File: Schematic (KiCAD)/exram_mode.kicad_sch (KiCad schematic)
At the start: 77 parts

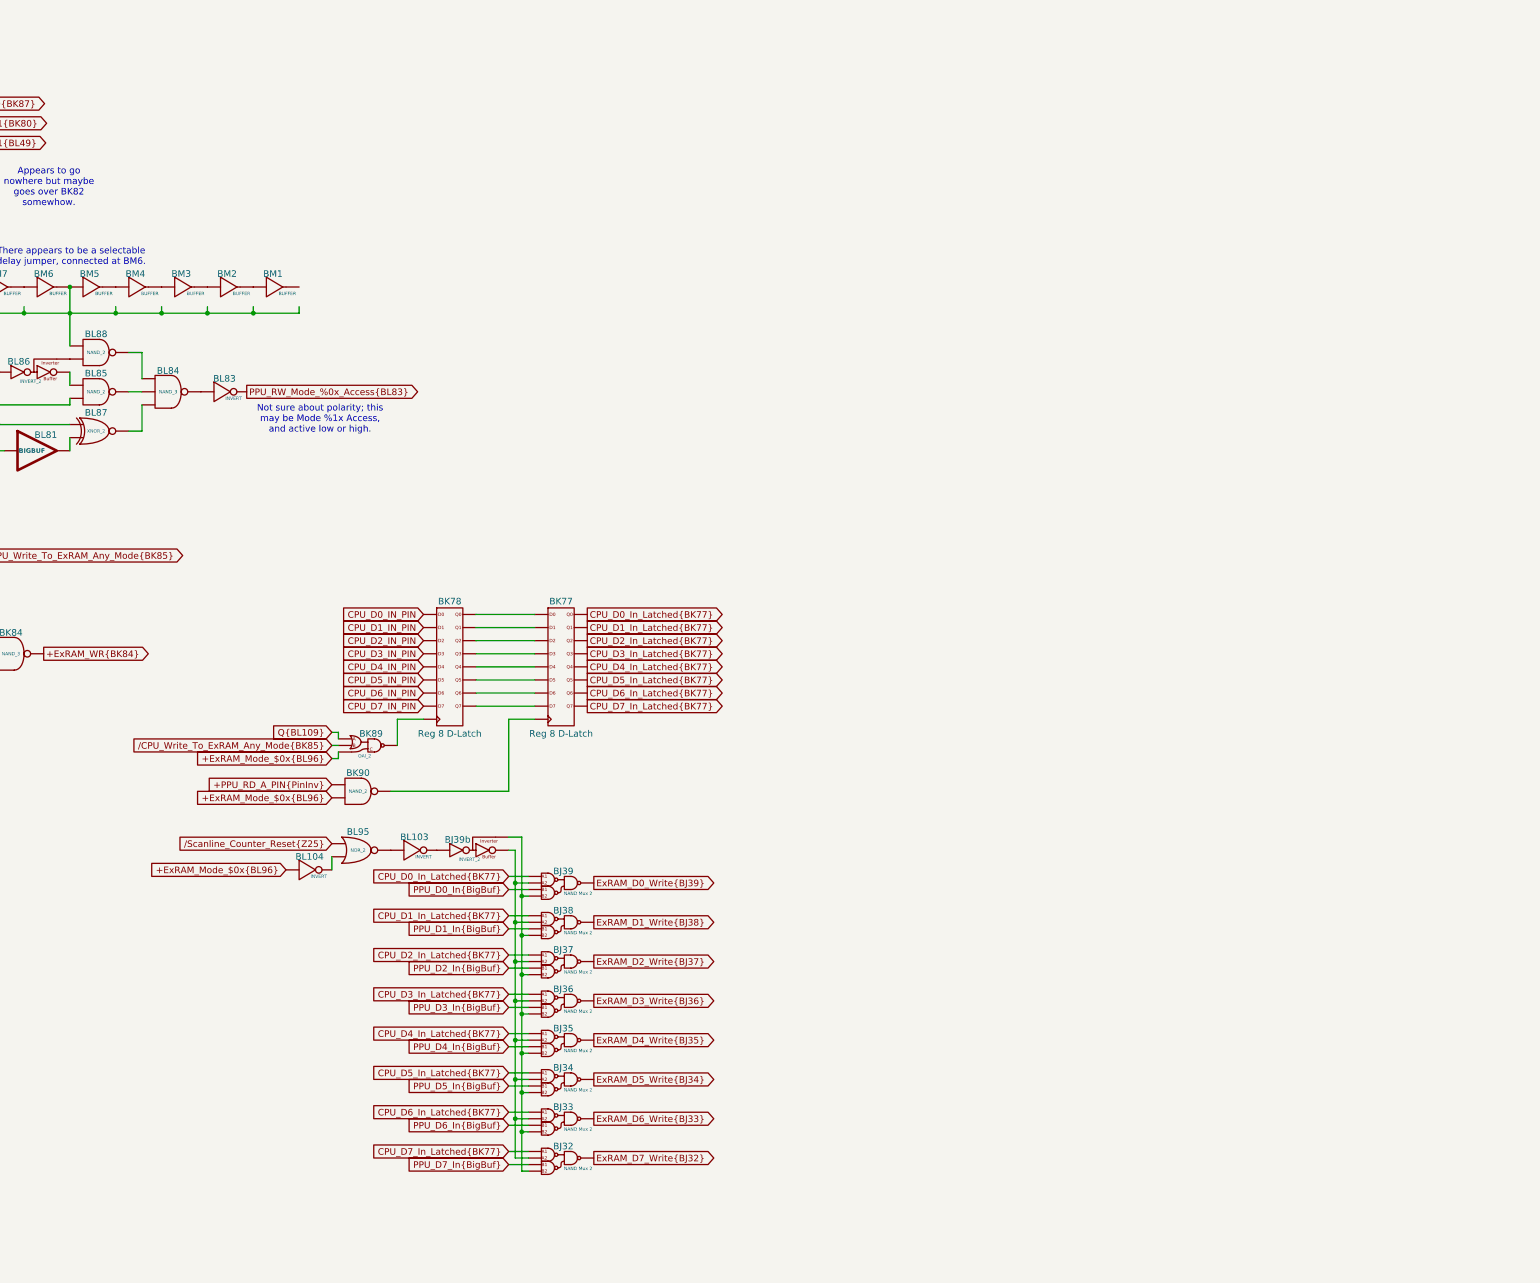
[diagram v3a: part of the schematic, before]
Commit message: - All known gates and traces are now accounted for in the schematics!  :)
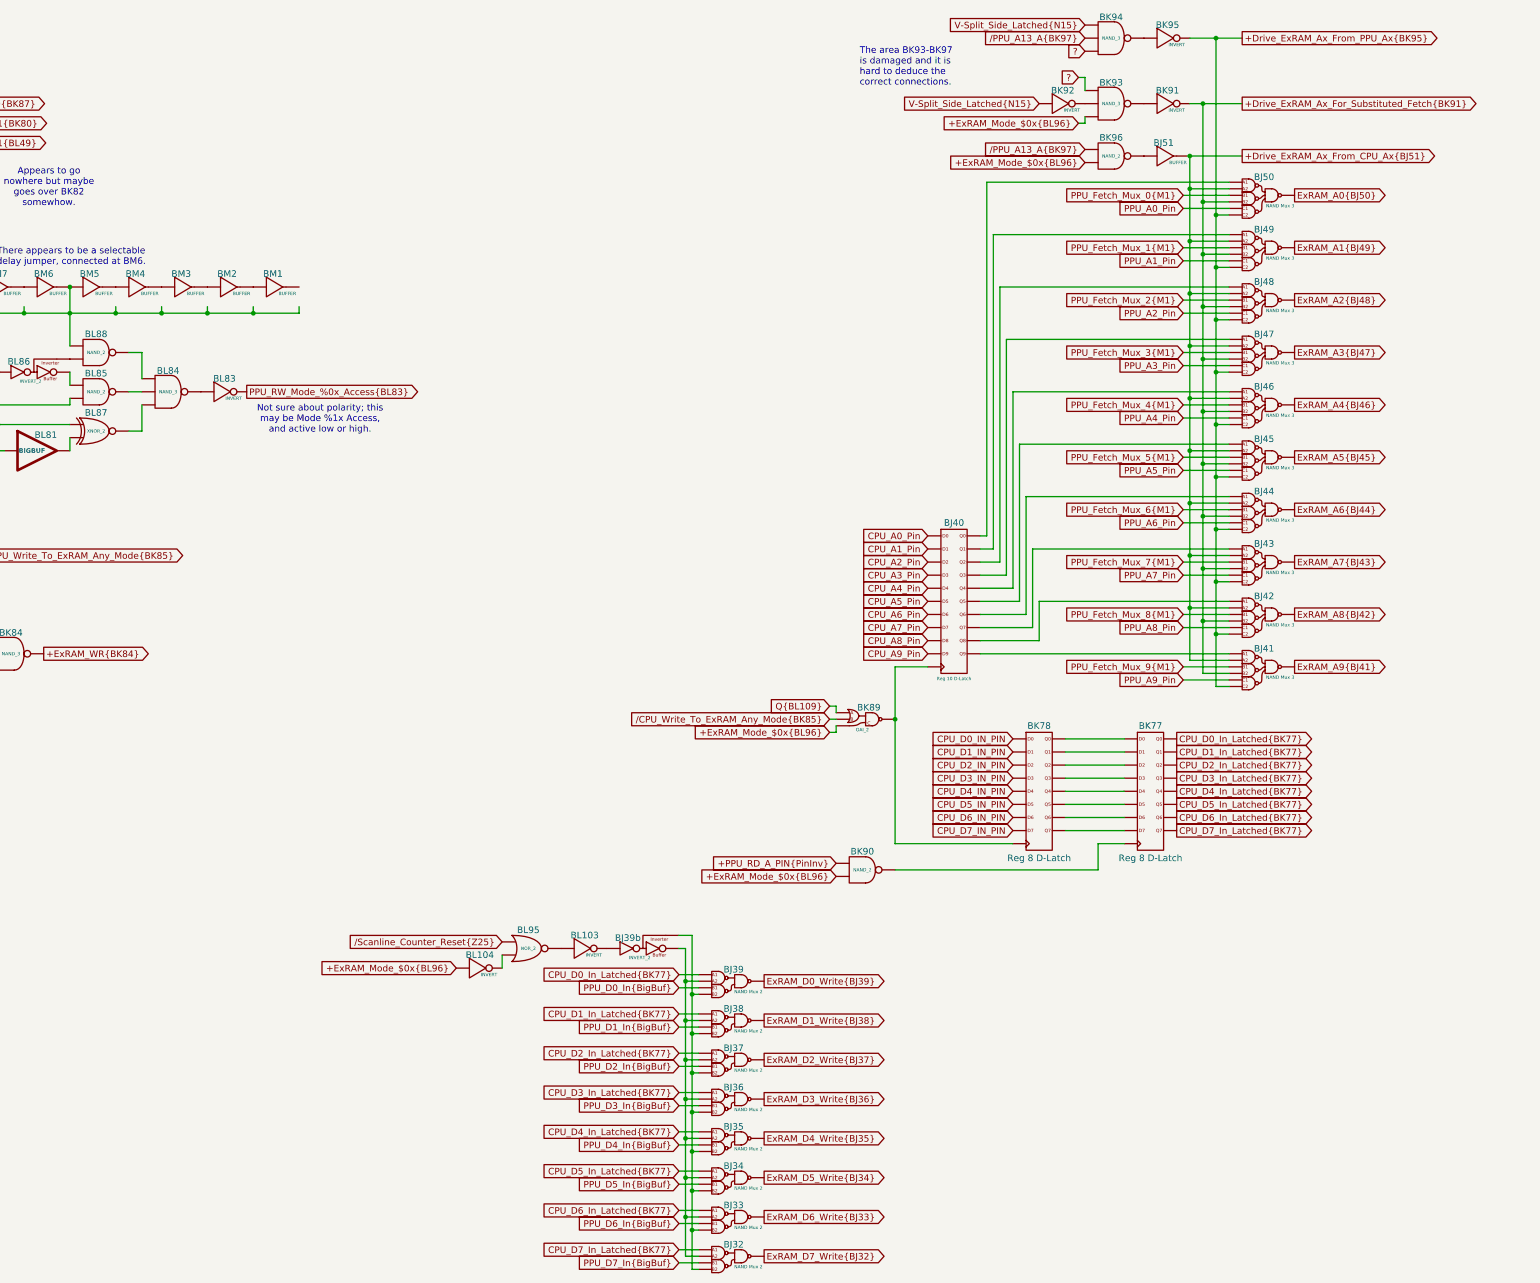
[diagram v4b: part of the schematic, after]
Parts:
- added BJ40: Reg 10 D-Latch, symbol MMC5:Reg_10_D-Latch
- added BJ41, BJ42, BJ43, BJ44, BJ45, BJ46, BJ47, BJ48, BJ49, BJ50: NAND Mux 3, symbol MMC5:NAND_Mux_3
- added BJ51: BUFFER, symbol MMC5:BUFFER
- added BK91, BK92, BK95: INVERT, symbol MMC5:INVERT
- added BK93, BK94: NAND_3, symbol MMC5:NAND_3
- added BK96: NAND_2, symbol MMC5:NAND_2
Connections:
- net +ExRAM_Mode_$0x{BL96}: now also BK93. (X), BK96. (X)
- net ?: now also BK93. (X), BK94. (X)
- net /PPU_A13_A{BK97}: now also BK94. (X), BK96. (X)
- net at BL100. (X): now also BL101. (X); no longer BL99. (/Q)
- net at BL90. (X): now also BL91. (X); no longer BL89. (/Q)
- net at BL93. (X): now also BL92. (X); no longer BN2. (X)
- net at BJ10. (X): now also BJ11. (/Q7); no longer BJ9. (X)
- net at BL88. (X): now also BL86. (X); no longer BL84. (X)
- net at BL92. (X): now also BL94. (X); no longer BL93. (X)
- net at BM9. (X): now also BM10. (X); no longer BM8. (X)
- net at BM10. (X): now also BL91. (X); no longer BM9. (X)
- net at BL84. (X): now also BL85. (X); no longer BL87. (X)
- net at BL103. (X): now also BJ39b. (X); no longer BL95. (X)
- net at BL85. (X): now also BL86. (X); no longer BL82. (X)
- net at BM3. (X): now also BM4. (X); no longer BM2. (X)
- net at BM4. (X): now also BM5. (X); no longer BM3. (X)
- net at BL106. (X): now also BL109. (/Q); no longer BL105. (X)
- new net: BL81. (X), BL87. (X)
- new net: BJ40. (Q9), BK78. (Q7), BK89. (X)
- new net: BK84. (X), BL102. (X), BL105. (X), BL107. (X), BN3. (X), BN4. (X)
- new net: BK83. (X), BK84. (X)
- new net: BK84. (X), BK86. (X)
- new net: BL102. (X), BL99. (/Q)
- new net: BL108. (X), BL99. (/Q)
- new net: BL100. (X), BL99. (/Q)
- new net: BL93. (X), BL94. (X), BL98. (/Q)
- new net: BL98. (/Q), BN1. (X)
- new net: BJ40. (Q9), BJ43. (X)
- new net: BK91. (X), BK93. (X)
- new net: BK77. (Q7), BK90. (X)
- new net: BK77. (Q7), BK78. (Q7) (x8)
- new net: BK79. (X), BK81. (X), BK82. (Q1)
- new net: BL89. (/Q), BL90. (X)
- new net: BK92. (X), BK93. (X)
- new net: BL93. (X), BN2. (X)
- new net: BJ7. (X), BJ9. (X)
- new net: BJ10. (X), BJ9. (X)
- new net: BJ32. (X), BJ33. (X), BJ34. (X), BJ35. (X), BJ36. (X), BJ37. (X), BJ38. (X), BJ39. (X), BJ39b. (X) (x2)
- new net: BL84. (X), BL88. (X)
- new net: BL88. (X), BM5. (X), BM6. (X)
- new net: BM8. (X), BM9. (X)
- new net: BK79. (X), BK82. (Q1), BL96. (X)
- new net: BL84. (X), BL87. (X)
- new net: BL104. (X), BL95. (X)
- new net: BL103. (X), BL95. (X)
- new net: BL82. (X), BL85. (X)
- new net: BL83. (X), BL84. (X)
- new net: BJ51. (X), BK96. (X)
- new net: BM2. (X), BM3. (X)
- new net: BK80. (X), BK82. (Q1)
- new net: BL105. (X), BL106. (X)
- new net: BL91. (X), BL92. (X)
- new net: BJ40. (Q9), BJ50. (X)
- new net: BJ40. (Q9), BJ46. (X)
- new net: BJ40. (Q9), BJ42. (X)
- new net: BJ40. (Q9), BJ44. (X)
- new net: BJ40. (Q9), BJ49. (X)
- new net: BJ40. (Q9), BJ45. (X)
- new net: BJ40. (Q9), BJ48. (X)
- new net: BJ40. (Q9), BJ47. (X)
- new net: BJ40. (Q9), BJ41. (X)
- new net: BK94. (X), BK95. (X)
- new net +Drive_ExRAM_Ax_For_Substituted_Fetch{BK91}: BJ41. (X), BJ42. (X), BJ43. (X), BJ44. (X), BJ45. (X), BJ46. (X), BJ47. (X), BJ48. (X), BJ49. (X), BJ50. (X), BK91. (X)
- new net +Drive_ExRAM_Ax_From_CPU_Ax{BJ51}: BJ41. (X), BJ42. (X), BJ43. (X), BJ44. (X), BJ45. (X), BJ46. (X), BJ47. (X), BJ48. (X), BJ49. (X), BJ50. (X), BJ51. (X)
- new net +Drive_ExRAM_Ax_From_PPU_Ax{BK95}: BJ41. (X), BJ42. (X), BJ43. (X), BJ44. (X), BJ45. (X), BJ46. (X), BJ47. (X), BJ48. (X), BJ49. (X), BJ50. (X), BK95. (X)
- new net CPU_A0_Pin: BJ40. (Q9)
- new net CPU_A1_Pin: BJ40. (Q9)
- new net CPU_A2_Pin: BJ40. (Q9)
- new net CPU_A3_Pin: BJ40. (Q9)
- new net CPU_A4_Pin: BJ40. (Q9)
- new net CPU_A5_Pin: BJ40. (Q9)
- new net CPU_A6_Pin: BJ40. (Q9)
- new net CPU_A7_Pin: BJ40. (Q9)
- new net CPU_A8_Pin: BJ40. (Q9)
- new net CPU_A9_Pin: BJ40. (Q9)
- new net ExRAM_A0{BJ50}: BJ50. (X)
- new net ExRAM_A1{BJ49}: BJ49. (X)
- new net ExRAM_A2{BJ48}: BJ48. (X)
- new net ExRAM_A3{BJ47}: BJ47. (X)
- new net ExRAM_A4{BJ46}: BJ46. (X)
- new net ExRAM_A5{BJ45}: BJ45. (X)
- new net ExRAM_A6{BJ44}: BJ44. (X)
- new net ExRAM_A7{BJ43}: BJ43. (X)
- new net ExRAM_A8{BJ42}: BJ42. (X)
- new net ExRAM_A9{BJ41}: BJ41. (X)
- new net PPU_A0_Pin: BJ50. (X)
- new net PPU_A1_Pin: BJ49. (X)
- new net PPU_A2_Pin: BJ48. (X)
- new net PPU_A3_Pin: BJ47. (X)
- new net PPU_A4_Pin: BJ46. (X)
- new net PPU_A5_Pin: BJ45. (X)
- new net PPU_A6_Pin: BJ44. (X)
- new net PPU_A7_Pin: BJ43. (X)
- new net PPU_A8_Pin: BJ42. (X)
- new net PPU_A9_Pin: BJ41. (X)
- new net PPU_Fetch_Mux_0{M1}: BJ50. (X)
- new net PPU_Fetch_Mux_1{M1}: BJ49. (X)
- new net PPU_Fetch_Mux_2{M1}: BJ48. (X)
- new net PPU_Fetch_Mux_3{M1}: BJ47. (X)
- new net PPU_Fetch_Mux_4{M1}: BJ46. (X)
- new net PPU_Fetch_Mux_5{M1}: BJ45. (X)
- new net PPU_Fetch_Mux_6{M1}: BJ44. (X)
- new net PPU_Fetch_Mux_7{M1}: BJ43. (X)
- new net PPU_Fetch_Mux_8{M1}: BJ42. (X)
- new net PPU_Fetch_Mux_9{M1}: BJ41. (X)
- new net V-Split_Side_Latched{N15}: BK92. (X), BK94. (X)
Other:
- note added: "The area BK93-BK97 is damaged and it is hard to deduce the correct connections."
- moved on the sheet: BJ32, BJ33, BJ34, BJ35, BJ36, BJ37, BJ38, BJ39, BJ39b, BK77, BK78, BK89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
